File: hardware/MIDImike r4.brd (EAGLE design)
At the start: 84.8 x 53.3 mm, 8 parts, among them SW1 PUSH-BTN, SW2 SH-7030TB

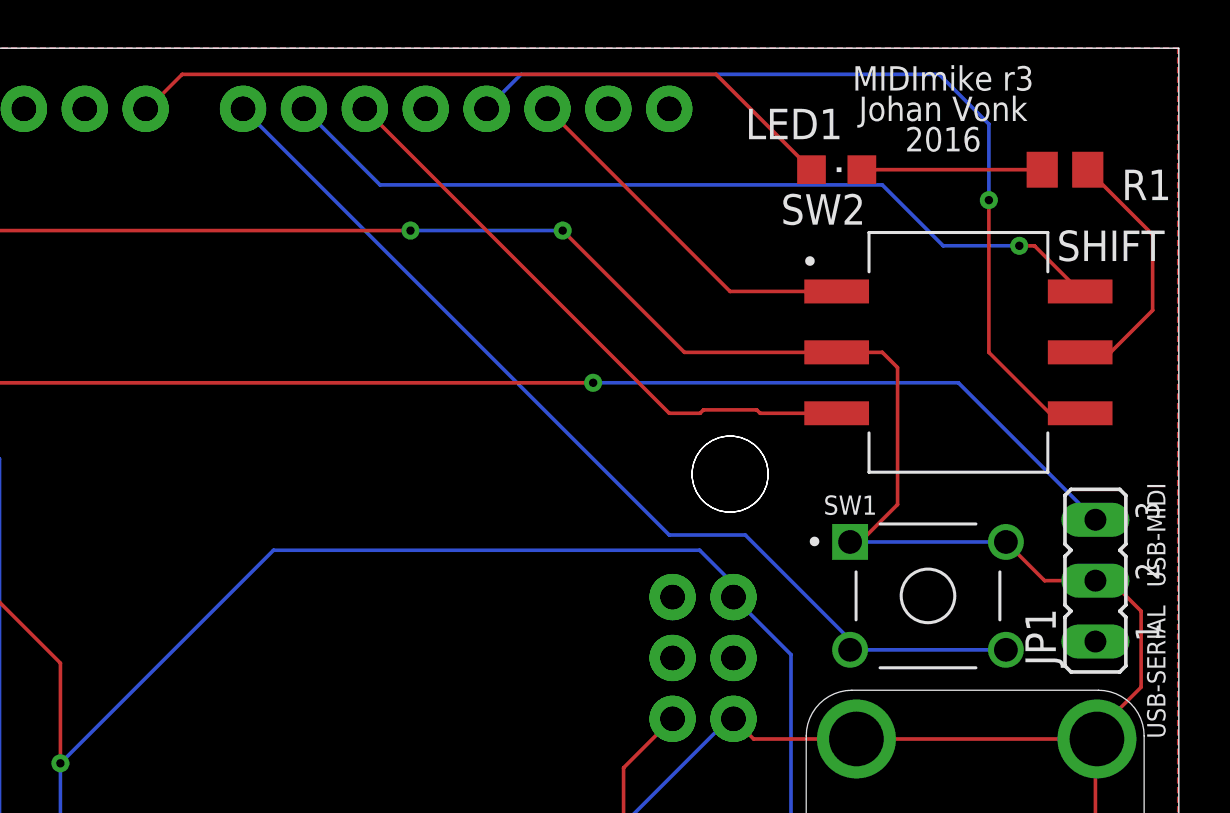
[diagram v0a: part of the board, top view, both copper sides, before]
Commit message: rm replay btn; mv clip led to D7
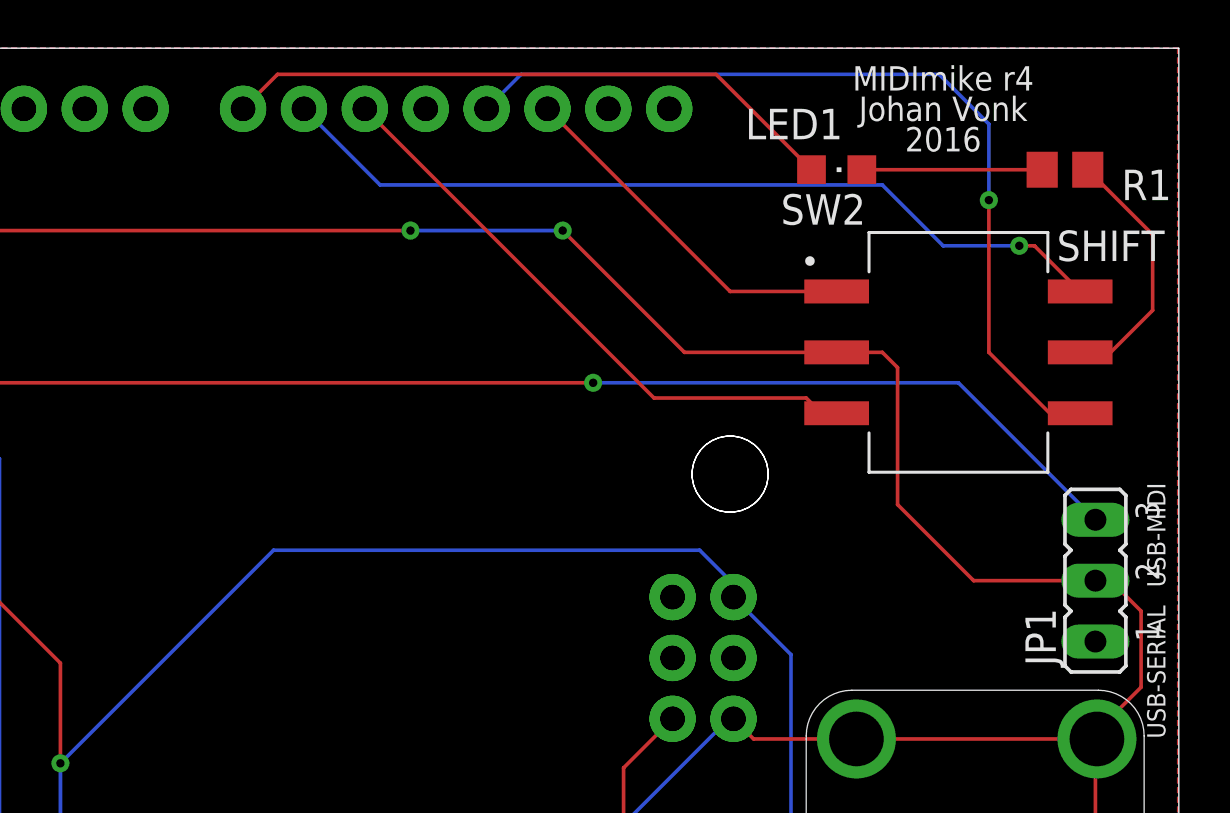
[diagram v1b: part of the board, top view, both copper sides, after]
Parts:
- removed SW1: PUSH-BTN, Coert-Vonk:TE_1-1825910-4
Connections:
- removed net D8: LED1.A, PCB2.D8
- new net N$11: PCB2.D8, PCB3.D8
- net D7: now also LED1.A; no longer SW1.2, SW1.2@1
- net GND: no longer SW1.1, SW1.1@1
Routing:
- net D8: track 30.0 -> 0.00 mm
- net D7: track 41.4 -> 26.0 mm
- net GND: track 187.6 -> 183.6 mm
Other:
- board text added: "MIDImike r4"
- board text removed: "MIDImike r3"
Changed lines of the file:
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@@
 <text x="83.82" y="33.02" size="0.762" layer="21" rot="R90" align="center">USB-MIDI</text>
 <text x="83.82" y="27.305" size="0.762" layer="21" rot="R90" align="center">USB-SERIAL</text>
-<text x="74.93" y="52.07" size="1.016" layer="21" align="center">MIDImike r3</text>
+<text x="74.93" y="52.07" size="1.016" layer="21" align="center">MIDImike r4</text>
 <text x="74.93" y="50.8" size="1.016" layer="21" align="center">Johan Vonk</text>
 <text x="74.93" y="49.53" size="1.016" layer="21" align="center">2016</text>
@@
 <attribute name="VALUE" x="33.02" y="-1.27" size="0.6096" layer="27" font="vector" ratio="20" align="top-center"/>
 </element>
-<element name="SW1" library="Coert-Vonk" package="TE_1-1825910-4" value="PUSH-BTN" x="74.295" y="30.48" smashed="yes">
-<attribute name="COMMENT" value="1-1825910-4" x="117.475" y="-91.44" size="1.778" layer="27" display="off"/>
-<attribute name="DESCRIPTION" value=" Switch Tactile OFF (ON) SPST Round Button PC Pins 0.05A 24VDC 100000Cycles 1.56N Thru-Hole " x="117.475" y="-91.44" size="1.778" layer="27" display="off"/>
-<attribute name="DIGI-KEY_PART_NUMBER" value="450-1653-ND" x="117.475" y="-91.44" size="1.778" layer="27" display="off"/>
-<attribute name="MF" value="TE Connectivity" x="117.475" y="-91.44" size="1.778" layer="27" display="off"/>
-<attribute name="MP" value="1-1825910-4" x="117.475" y="-91.44" size="1.778" layer="27" display="off"/>
-<attribute name="NAME" x="69.93791875" y="33.866059375" size="0.80100625" layer="25"/>
-<attribute name="PACKAGE" value="None" x="117.475" y="-91.44" size="1.778" layer="27" display="off"/>
-<attribute name="PURCHASE-URL" value="https://pricing.snapeda.com/search/part/1-1825910-4/?ref=eda" x="117.475" y="-91.44" size="1.778" layer="27" display="off"/>
-<attribute name="VALUE" x="69.864490625" y="26.11893125" size="0.800415625" layer="27"/>
-</element>
 <element name="JP1" library="Coert-Vonk" package="JP2" package3d_urn="urn:adsk.eagle:package:15452/1" value="" x="81.28" y="31.115" smashed="yes" rot="R90">
 <attribute name="NAME" x="79.629" y="27.559" size="1.27" layer="25" ratio="10" rot="R90"/>
@@
 <contactref element="R1" pad="1"/>
 <contactref element="PCB1" pad="3"/>
-<contactref element="SW1" pad="1"/>
-<contactref element="SW1" pad="1@1"/>
 <contactref element="SW2" pad="C_2" route="any" routetag="G$1.C"/>
 <contactref element="SW2" pad="C_1" route="any" routetag="G$1.C"/>
@@
 <wire x1="83.185" y1="29.845" x2="81.915" y2="31.115" width="0.1524" layer="1"/>
 <wire x1="81.915" y1="31.115" x2="81.28" y2="31.115" width="0.1524" layer="1"/>
-<wire x1="81.28" y1="31.115" x2="79.16" y2="31.115" width="0.1524" layer="1"/>
-<wire x1="79.16" y1="31.115" x2="77.545" y2="32.73" width="0.1524" layer="1"/>
-<wire x1="71.045" y1="32.73" x2="77.545" y2="32.73" width="0.1524" layer="16"/>
 <wire x1="71.3105" y1="24.511" x2="81.2165" y2="24.511" width="0.1524" layer="1"/>
 <wire x1="81.2165" y1="24.511" x2="81.28" y2="24.4475" width="0.1524" layer="1"/>
 <wire x1="66.18000625" y1="25.3499875" x2="67.01899375" y2="24.511" width="0.1524" layer="1"/>
 <wire x1="67.01899375" y1="24.511" x2="71.3105" y2="24.511" width="0.1524" layer="1"/>
-<wire x1="73.025" y1="34.29" x2="71.465" y2="32.73" width="0.1524" layer="1"/>
-<wire x1="71.465" y1="32.73" x2="71.045" y2="32.73" width="0.1524" layer="1"/>
 <wire x1="83.6678" y1="45.5522" x2="80.96" y2="48.26" width="0.1524" layer="1"/>
 <wire x1="83.6678" y1="42.3928" x2="83.6678" y2="45.5522" width="0.1524" layer="1"/>
@@
 <wire x1="70.485" y1="40.64" x2="72.39" y2="40.64" width="0.1524" layer="1"/>
 <wire x1="72.39" y1="40.64" x2="73.025" y2="40.005" width="0.1524" layer="1"/>
-<wire x1="73.025" y1="40.005" x2="73.025" y2="34.29" width="0.1524" layer="1"/>
+<wire x1="73.025" y1="34.29" x2="73.025" y2="40.005" width="0.1524" layer="1"/>
 <wire x1="70.485" y1="40.64" x2="64.135" y2="40.64" width="0.1524" layer="1"/>
 <wire x1="80.645" y1="40.64" x2="81.915" y2="40.64" width="0.1524" layer="1"/>
 <wire x1="81.915" y1="40.64" x2="83.6678" y2="42.3928" width="0.1524" layer="1"/>
+<wire x1="81.28" y1="31.115" x2="76.2" y2="31.115" width="0.1524" layer="1"/>
+<wire x1="76.2" y1="31.115" x2="73.025" y2="34.29" width="0.1524" layer="1"/>
 </signal>
 <signal name="5V">
@@
 <wire x1="71.535" y1="48.26" x2="79.06" y2="48.26" width="0.1524" layer="1"/>
 </signal>
-<signal name="D8">
-<contactref element="LED1" pad="A"/>
-<contactref element="PCB2" pad="D8"/>
-<wire x1="69.435" y1="48.26" x2="65.4572" y2="52.2378" width="0.1524" layer="1"/>
-<wire x1="41.656" y1="50.8" x2="41.7422" y2="50.8" width="0.1524" layer="1"/>
-<wire x1="43.18" y1="52.2378" x2="41.7422" y2="50.8" width="0.1524" layer="1"/>
-<wire x1="65.4572" y1="52.2378" x2="43.18" y2="52.2378" width="0.1524" layer="1"/>
-</signal>
 <signal name="N$13">
 <contactref element="PCB2" pad="D5"/>
 <contactref element="SW2" pad="4"/>
-<wire x1="63.5" y1="38.1" x2="50.8" y2="50.8" width="0.1524" layer="1"/>
-<wire x1="70.485" y1="38.1" x2="67.28966875" y2="38.1" width="0.1524" layer="1"/>
-<wire x1="67.28966875" y1="38.1" x2="67.14996875" y2="38.2397" width="0.1524" layer="1"/>
-<wire x1="67.14996875" y1="38.2397" x2="64.93003125" y2="38.2397" width="0.1524" layer="1"/>
-<wire x1="64.93003125" y1="38.2397" x2="64.79033125" y2="38.1" width="0.1524" layer="1"/>
-<wire x1="64.79033125" y1="38.1" x2="63.5" y2="38.1" width="0.1524" layer="1"/>
+<wire x1="69.215" y1="38.735" x2="69.8246" y2="38.1254" width="0.1524" layer="1"/>
+<wire x1="69.8246" y1="38.1254" x2="69.85" y2="38.1" width="0.1524" layer="1"/>
+<wire x1="50.8" y1="50.8" x2="62.865" y2="38.735" width="0.1524" layer="1"/>
+<wire x1="62.865" y1="38.735" x2="69.215" y2="38.735" width="0.1524" layer="1"/>
+<wire x1="69.7992" y1="38.1" x2="70.485" y2="38.1" width="0.1524" layer="1"/>
+<wire x1="69.7992" y1="38.1" x2="69.8246" y2="38.1254" width="0.1524" layer="1"/>
 </signal>
 <signal name="N$14">
@@
 <signal name="D7">
 <contactref element="PCB2" pad="D7"/>
-<contactref element="SW1" pad="2@1"/>
-<contactref element="SW1" pad="2"/>
-<wire x1="45.72" y1="50.8" x2="63.5" y2="33.02" width="0.1524" layer="16"/>
-<wire x1="63.5" y1="33.02" x2="66.675" y2="33.02" width="0.1524" layer="16"/>
-<wire x1="66.675" y1="33.02" x2="71.045" y2="28.65" width="0.1524" layer="16"/>
-<wire x1="71.045" y1="28.65" x2="71.045" y2="28.23" width="0.1524" layer="16"/>
-<wire x1="77.545" y1="28.23" x2="71.045" y2="28.23" width="0.1524" layer="16"/>
+<contactref element="LED1" pad="A"/>
+<wire x1="65.4572" y1="52.2378" x2="69.435" y2="48.26" width="0.1524" layer="1"/>
+<wire x1="45.72" y1="50.8" x2="47.1578" y2="52.2378" width="0.1524" layer="1"/>
+<wire x1="47.1578" y1="52.2378" x2="65.4572" y2="52.2378" width="0.1524" layer="1"/>
 </signal>
 <signal name="N$1">
@@
 <wire x1="22.9862125" y1="47.4987875" x2="26.035" y2="44.45" width="0.1524" layer="16"/>
 </signal>
+<signal name="N$11">
+<contactref element="PCB2" pad="D8"/>
+<contactref element="PCB3" pad="D8"/>
+</signal>
 </signals>
